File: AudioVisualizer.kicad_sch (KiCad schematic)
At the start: 317 parts, among them J1 AudioJack3, J2 AudioJack3, J3 Barrel_Jack_Switch_Pin3Ring, U1 LM2904, U10 LM393, U11 LM393, U12 LM393, U13 LM393, U14 LM393, U15 LM393, U16 LM393, U17 LM393, U18 LM393, U19 LM393, U2 LM2904, U20 LM393, U21 LM393, U22 LM393, U23 LM393, U24 LM393, U25 LM393, U26 LM393, U27 LM393, U28 LM393, U29 LM393, U3 LM2904, U30 LM393, U31 LM393, U32 LM393, U33 LM393, U34 LM393, U35 LM393, U36 LM393, U37 LM393, U38 LM393, U39 LM393, U4 LM2904, U40 LM393, U41 LM393, U42 LM393, U43 LM393, U44 LM393, U45 LM393, U46 LM393, U47 LM393, U48 LM393, U49 LM393, U5 LM2904, U50 LM393, U51 LM393, U52 LM393, U53 LM393, U54 L7805, U6 LM393, U7 LM393, U8 LM393, U9 LM393

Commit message: 回路修正，基板修正
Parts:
- added C25: 0.1uF, Capacitor_THT:C_Disc_D5.0mm_W2.5mm_P5.00mm, symbol Device:C
- C20: value 0.047uF -> 0.01uF
- C23: value 0.1uF -> 0.047uF
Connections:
- net +12V: now also C24.1; no longer C23.1
- net +5V: now also C25.1; no longer C24.1
- net Band-7: now also C20.1; no longer C19.2
- net BufferOut: now also C22.1; no longer C21.1
- net GND: now also C25.2; no longer C23.2
- net at R28.2, U5.2 (-): now also C21.2; no longer C20.1
- net at C19.1, R26.2, R27.1: now also C21.1; no longer C20.2
- net at R30.1, U5.5 (+): now also C23.2; no longer C22.2
- new net: C22.2, C23.1, R29.1
- new net: C19.2, C20.2

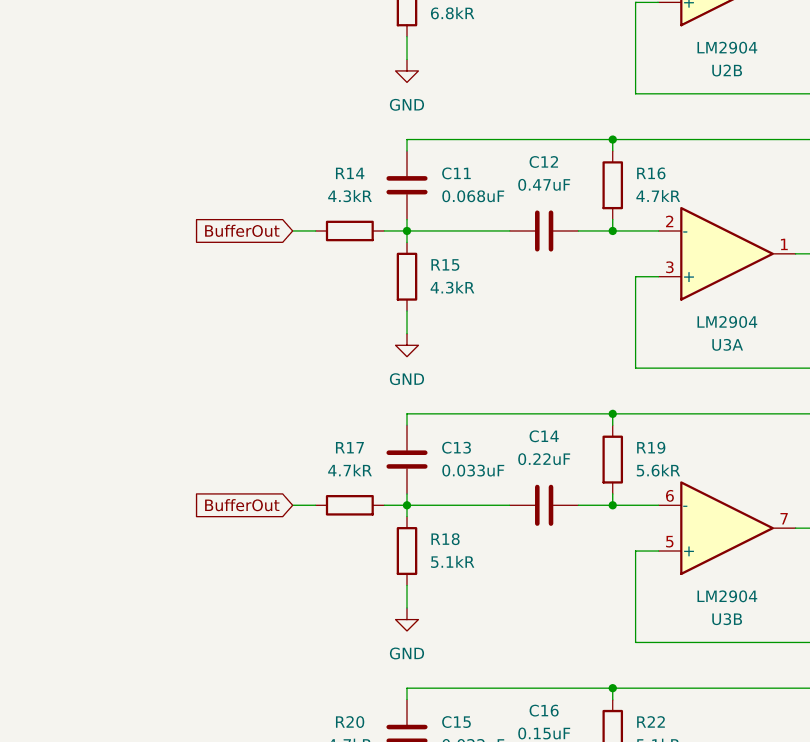
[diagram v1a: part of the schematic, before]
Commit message: 抵抗値修正
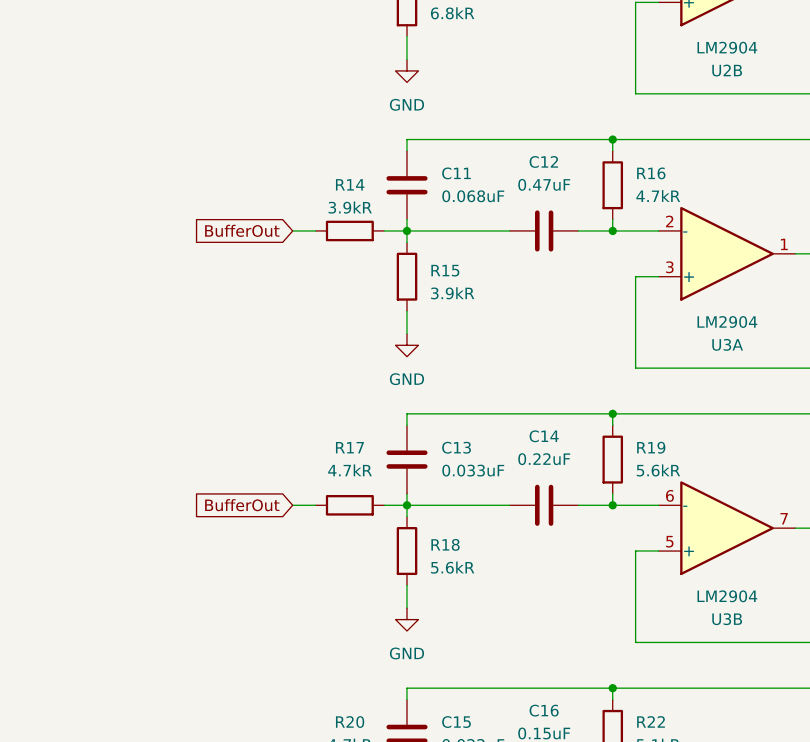
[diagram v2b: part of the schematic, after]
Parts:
- R14, R15: value 4.3kR -> 3.9kR
- R18: value 5.1kR -> 5.6kR
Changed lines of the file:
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@@
   (symbol (lib_id "Device:R") (at 313.69 213.36 0) (unit 1)
     (in_bom yes) (on_board yes) (dnp no) (fields_autoplaced)
-    (property "Reference" "R15" (at 316.23 212.09 0)
+    (property "Reference" "R15" (at 316.23 212.725 0)
       (effects (font (size 1.27 1.27)) (justify left))
     )
-    (property "Value" "4.3kR" (at 316.23 214.63 0)
+    (property "Value" "3.9kR" (at 316.23 215.265 0)
       (effects (font (size 1.27 1.27)) (justify left))
     )
@@
   (symbol (lib_id "Device:R") (at 313.69 243.84 0) (unit 1)
     (in_bom yes) (on_board yes) (dnp no) (fields_autoplaced)
-    (property "Reference" "R18" (at 316.23 242.57 0)
+    (property "Reference" "R18" (at 316.23 243.205 0)
       (effects (font (size 1.27 1.27)) (justify left))
     )
-    (property "Value" "5.1kR" (at 316.23 245.11 0)
+    (property "Value" "5.6kR" (at 316.23 245.745 0)
       (effects (font (size 1.27 1.27)) (justify left))
     )
@@
   (symbol (lib_id "Device:R") (at 307.34 208.28 90) (unit 1)
     (in_bom yes) (on_board yes) (dnp no) (fields_autoplaced)
-    (property "Reference" "R14" (at 307.34 201.93 90)
+    (property "Reference" "R14" (at 307.34 203.2 90)
       (effects (font (size 1.27 1.27)))
     )
-    (property "Value" "4.3kR" (at 307.34 204.47 90)
+    (property "Value" "3.9kR" (at 307.34 205.74 90)
       (effects (font (size 1.27 1.27)))
     )

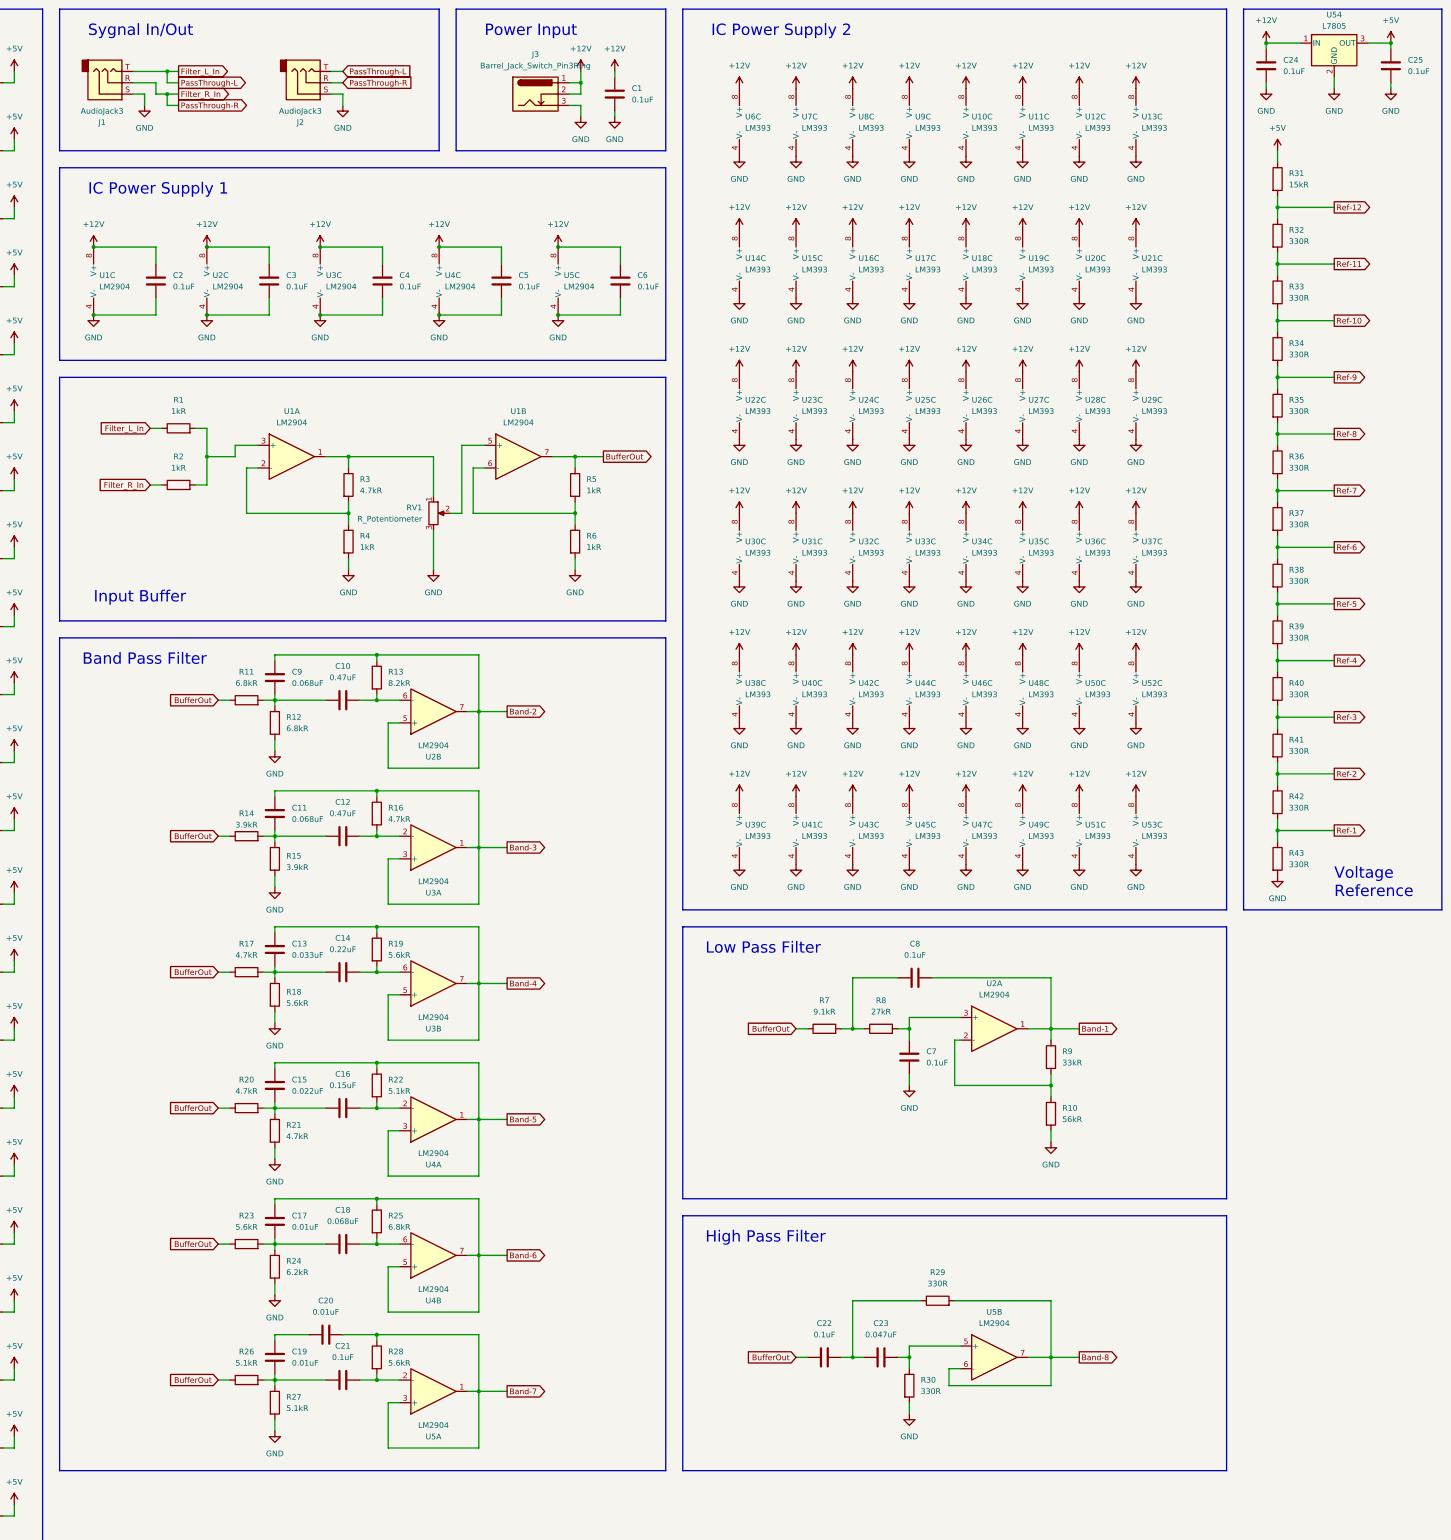
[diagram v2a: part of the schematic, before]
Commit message: update to log scale || fix filter circuit
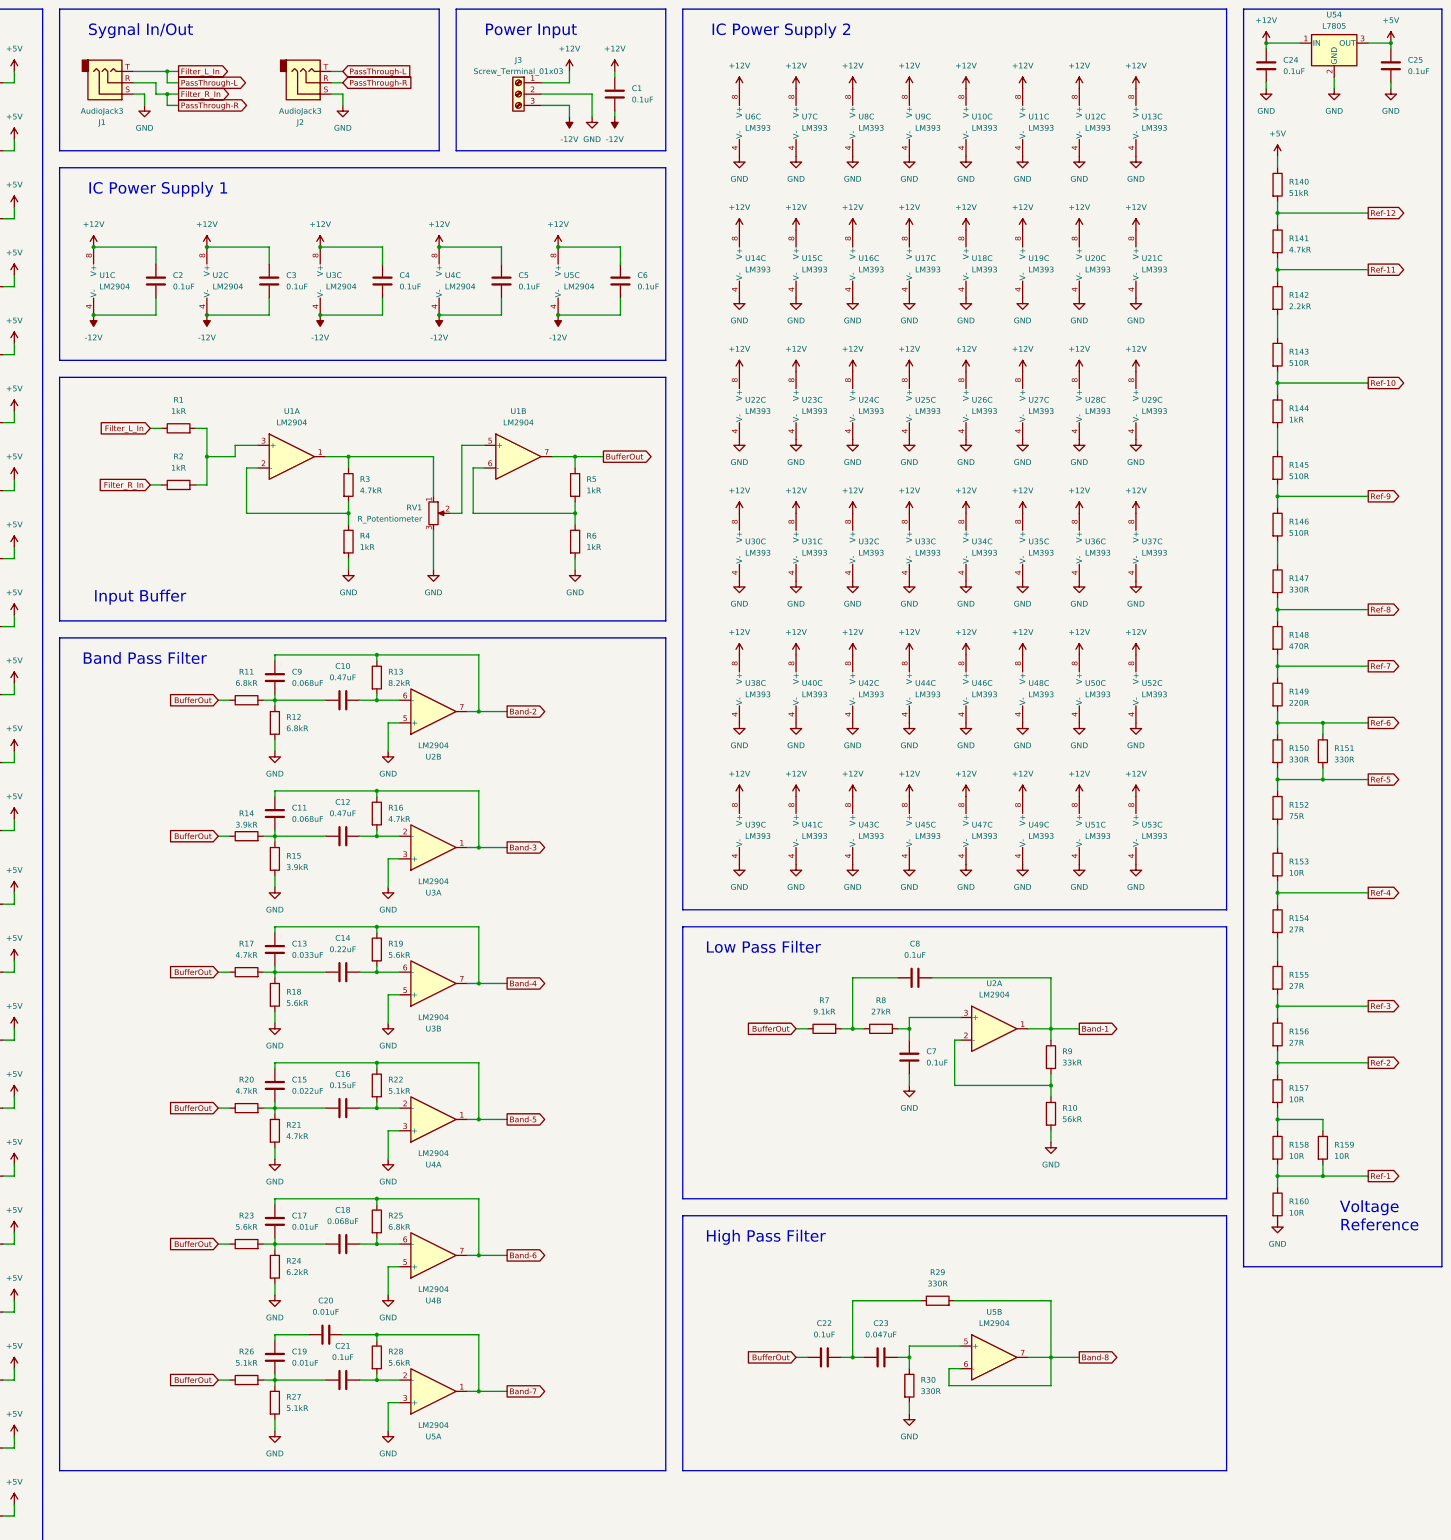
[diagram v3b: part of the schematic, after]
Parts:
- removed J3: Barrel_Jack_Switch_Pin3Ring, Connector_BarrelJack:BarrelJack_Horizontal, symbol Connector:Barrel_Jack_Switch_Pin3Ring
- removed R31: 15kR, Resistor_THT:R_Axial_DIN0204_L3.6mm_D1.6mm_P7.62mm_Horizontal, symbol Device:R
- removed R32, R33, R34, R35, R36, R37, R38, R39, R40, R41, R42, R43: 330R, Resistor_THT:R_Axial_DIN0204_L3.6mm_D1.6mm_P7.62mm_Horizontal, symbol Device:R
- added J3: Screw_Terminal_01x03, TerminalBlock:TerminalBlock_bornier-3_P5.08mm, symbol Connector:Screw_Terminal_01x03
- added R140: 51kR, Resistor_THT:R_Axial_DIN0204_L3.6mm_D1.6mm_P7.62mm_Horizontal, symbol Device:R
- added R141: 4.7kR, Resistor_THT:R_Axial_DIN0204_L3.6mm_D1.6mm_P7.62mm_Horizontal, symbol Device:R
- added R142: 2.2kR, Resistor_THT:R_Axial_DIN0204_L3.6mm_D1.6mm_P7.62mm_Horizontal, symbol Device:R
- added R143, R145, R146: 510R, Resistor_THT:R_Axial_DIN0204_L3.6mm_D1.6mm_P7.62mm_Horizontal, symbol Device:R
- added R144: 1kR, Resistor_THT:R_Axial_DIN0204_L3.6mm_D1.6mm_P7.62mm_Horizontal, symbol Device:R
- added R147, R150, R151: 330R, Resistor_THT:R_Axial_DIN0204_L3.6mm_D1.6mm_P7.62mm_Horizontal, symbol Device:R
- added R148: 470R, Resistor_THT:R_Axial_DIN0204_L3.6mm_D1.6mm_P7.62mm_Horizontal, symbol Device:R
- added R149: 220R, Resistor_THT:R_Axial_DIN0204_L3.6mm_D1.6mm_P7.62mm_Horizontal, symbol Device:R
- added R152: 75R, Resistor_THT:R_Axial_DIN0204_L3.6mm_D1.6mm_P7.62mm_Horizontal, symbol Device:R
- added R153, R157, R158, R159, R160: 10R, Resistor_THT:R_Axial_DIN0204_L3.6mm_D1.6mm_P7.62mm_Horizontal, symbol Device:R
- added R154, R155, R156: 27R, Resistor_THT:R_Axial_DIN0204_L3.6mm_D1.6mm_P7.62mm_Horizontal, symbol Device:R
- RV1: footprint Potentiometer_THT:Potentiometer_Bourns_3386P_Vertical -> Connector_PinHeader_2.54mm:PinHeader_1x03_P2.54mm_Vertical
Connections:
- net +12V: now also J3.1 (Pin_1)
- net +5V: now also R140.1
- net Band-2: no longer U2.5 (+)
- net Band-3: no longer U3.3 (+)
- net Band-4: no longer U3.5 (+)
- net Band-5: no longer U4.3 (+)
- net Band-6: no longer U4.5 (+)
- net Band-7: no longer U5.3 (+)
- net GND: now also U2.5 (+), U3.3 (+), U3.5 (+), U4.3 (+), U4.5 (+), U5.3 (+), J3.2 (Pin_2), R160.2; no longer C1.2, C2.2, C3.2, C4.2, C5.2, C6.2, U1.4 (V-), U2.4 (V-), U3.4 (V-), U4.4 (V-), U5.4 (V-)
- net Ref-1: now also R158.2, R159.2, R160.1
- net Ref-10: now also R143.2, R144.1
- net Ref-11: now also R141.2, R142.1
- net Ref-12: now also R140.2, R141.1
- net Ref-2: now also R156.2, R157.1
- net Ref-3: now also R155.2, R156.1
- net Ref-4: now also R153.2, R154.1
- net Ref-5: now also R150.2, R151.2, R152.1
- net Ref-6: now also R149.2, R150.1, R151.1
- net Ref-7: now also R148.2, R149.1
- net Ref-8: now also R147.2, R148.1
- net Ref-9: now also R145.2, R146.1
- new net: R144.2, R145.1
- new net: R146.2, R147.1
- new net: R142.2, R143.1
- new net: R157.2, R158.1, R159.1
- new net: R154.2, R155.1
- new net: R152.2, R153.1
- new net -12V: C1.2, C2.2, C3.2, C4.2, C5.2, C6.2, J3.3 (Pin_3), U1.4 (V-), U2.4 (V-), U3.4 (V-), U4.4 (V-), U5.4 (V-)

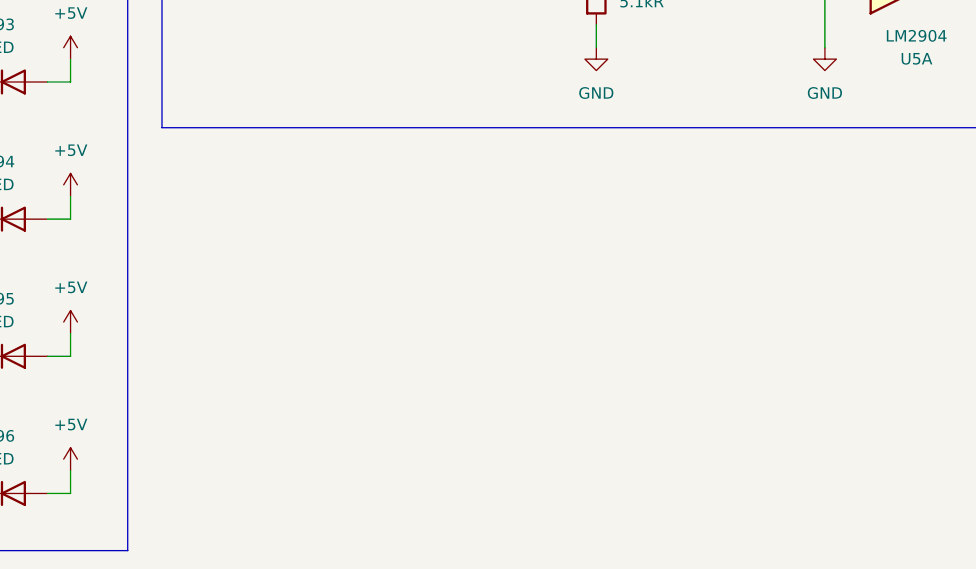
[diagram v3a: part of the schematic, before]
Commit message: add usb power out
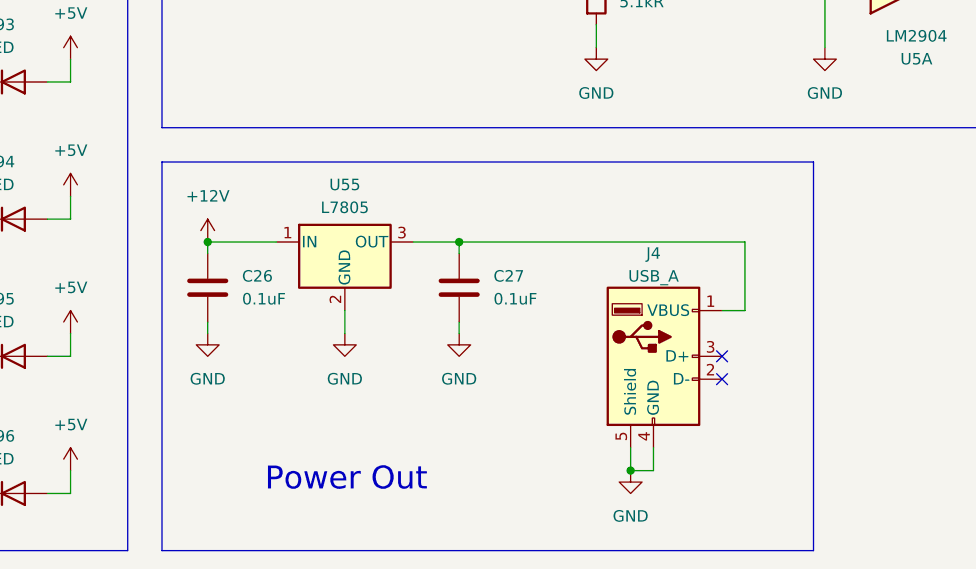
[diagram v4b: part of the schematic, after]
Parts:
- added C26, C27: 0.1uF, Capacitor_THT:C_Disc_D5.0mm_W2.5mm_P5.00mm, symbol Device:C
- added J4: USB_A, Connector_USB:USB_A_CONNFLY_DS1095-WNR0, symbol Connector:USB_A
- added U55: L7805, Package_TO_SOT_THT:TO-220-3_Vertical, symbol Regulator_Linear:L7805
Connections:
- net +12V: now also C26.1, U55.1 (IN)
- net GND: now also C26.2, C27.2, J4.4 (GND), J4.5 (Shield), U55.2 (GND)
- new net: C27.1, J4.1 (VBUS), U55.3 (OUT)
- no-connect marks 0 -> 2
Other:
- note added: "Power Out"

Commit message: Q 値を調整
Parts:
- removed C21: 0.1uF, Capacitor_THT:C_Disc_D5.0mm_W2.5mm_P5.00mm, symbol Device:C
- removed R10: 56kR, Resistor_THT:R_Axial_DIN0204_L3.6mm_D1.6mm_P7.62mm_Horizontal, symbol Device:R
- removed R9: 33kR, Resistor_THT:R_Axial_DIN0204_L3.6mm_D1.6mm_P7.62mm_Horizontal, symbol Device:R
- C10: value 0.47uF -> 0.047uF
- C11: value 0.068uF -> 0.68uF
- C12: value 0.47uF -> 0.033uF
- C13: value 0.033uF -> 0.33uF
- C14: value 0.22uF -> 0.015uF
- C15: value 0.022uF -> 0.22uF
- C16: value 0.15uF -> 0.0068uF
- C17: value 0.01uF -> 0.15uF
- C18: value 0.068uF -> 0.0068uF
- C19: value 0.01uF -> 0.068uF
- C20: value 0.01uF -> 0.0033uF
- C21: renamed from C22; value 0.1uF -> 0.001uF
- C22: renamed from C23; value 0.047uF -> 0.001uF
- C7: value 0.1uF -> 0.0068uF
- C8: value 0.1uF -> 1uF
- C9: value 0.068uF -> 1uF
- R11: value 6.8kR -> 5.6kR
- R12: value 6.8kR -> 150R
- R13: value 8.2kR -> 150kR
- R14: value 3.9kR -> 5.1kR
- R15: value 3.9kR -> 130R
- R16: value 4.7kR -> 100kR
- R17, R20: value 4.7kR -> 5.6kR
- R18: value 5.6kR -> 150R
- R19, R28: value 5.6kR -> 150kR
- R21: value 4.7kR -> 150R
- R22: value 5.1kR -> 180kR
- R23: value 5.6kR -> 4.7kR
- R24: value 6.2kR -> 120R
- R25: value 6.8kR -> 100kR
- R26: value 5.1kR -> 6.2kR
- R27: value 5.1kR -> 150R
- R29: value 330R -> 2.7kR
- R30: value 330R -> 390R
- R7: value 9.1kR -> 22kR
- R8: value 27kR -> 15kR
- renumbered C24 to C23, C25 to C24, C26 to C25, C27 to C26
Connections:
- net Band-1: now also U2.2 (-)
- net Band-7: now also C19.2; no longer C20.1
- net at R28.2, U5.2 (-): now also C20.1
- net at C19.1, R26.2, R27.1: now also C20.2
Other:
- note added: "102Hz, Q = 5.98"
- note added: "1456Hz, Q = 5.95"
- note added: "156Hz, Q = 6.63"
- note added: "2528Hz, Q = 7.50"
- note added: "298Hz, Q = 5.90"
- note added: "483Hz, Q = 6.53"
- note added: "4904Hz, Q = 6.00"
- note added: "802Hz, Q = 5.98"
